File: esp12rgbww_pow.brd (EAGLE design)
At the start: 31.5 x 30 mm, 16 parts, among them J1 1X2-3.5MM, J2 1X2-3.5MM, J3 1X2-3.5MM

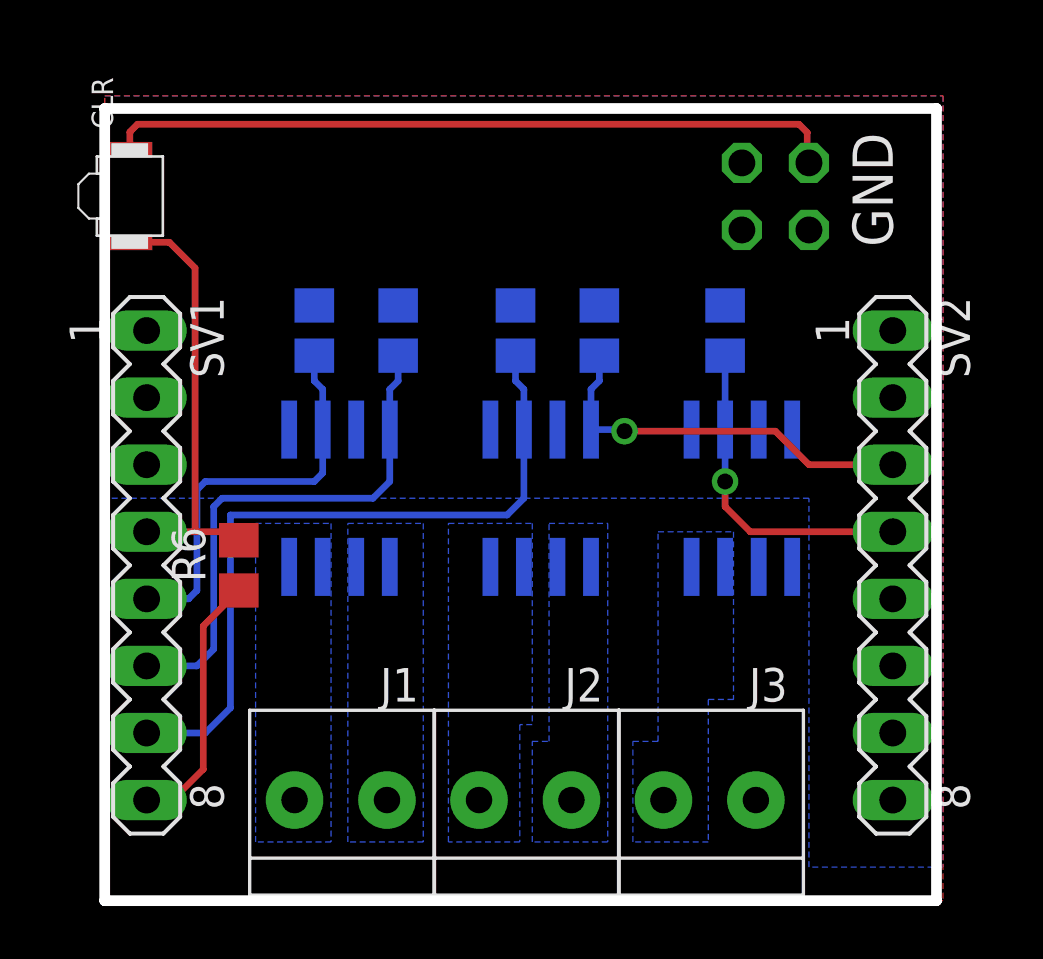
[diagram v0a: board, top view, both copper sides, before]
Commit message: FT232 module
FT232 Module now functional as a prototype
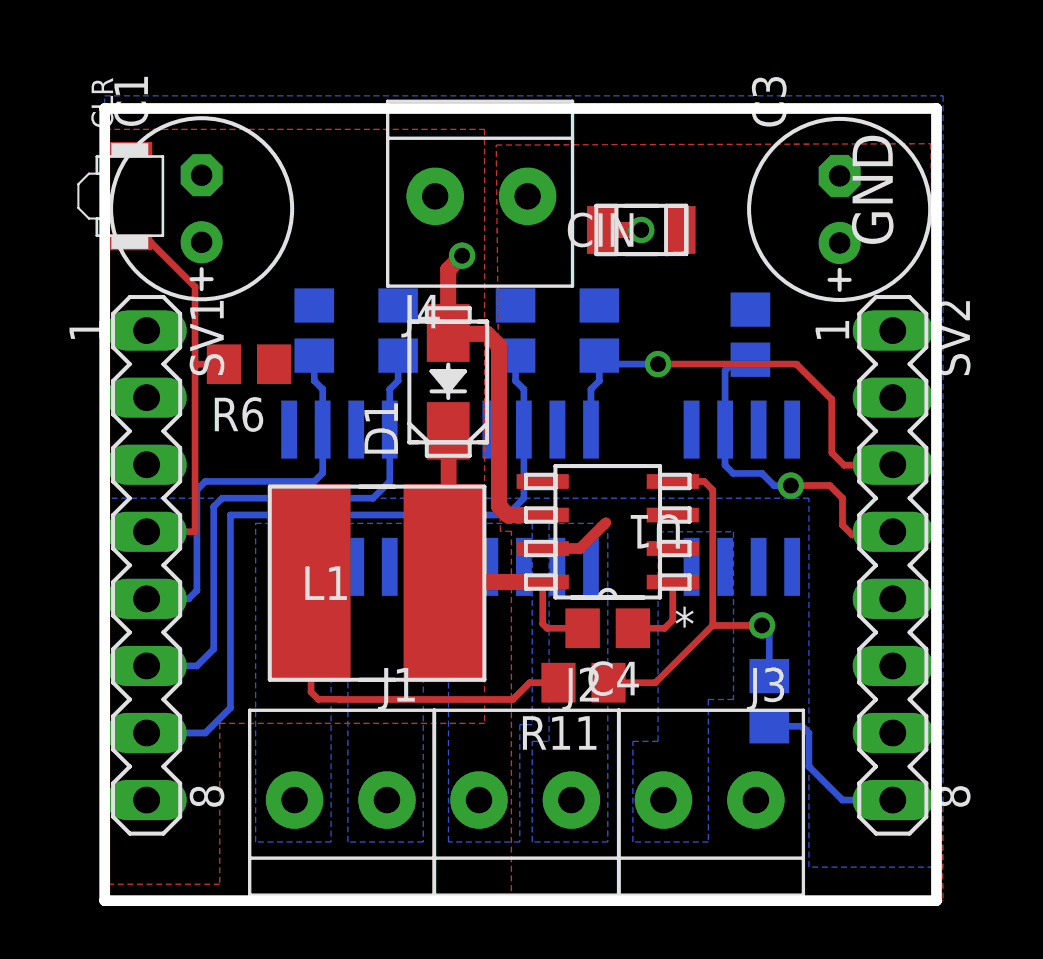
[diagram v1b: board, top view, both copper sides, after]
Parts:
- removed JP1: (no value), pinhead:2X02
- added C1: 440nF, resistor:E2,5-7
- added C3: 240uF, resistor:E2,5-7
- added C4: 10nF, resistor:C0805
- added CIN: 4.7uF, AcceleratedDesigns_Lib:1206
- added D1: 570mV, TI_Accelerated_Design_neu:SMA
- added J4: 1X2-3.5MM, adafruit:1X2-3.5MM
- added L1: 56uH, AcceleratedDesigns_Lib:IND_NPI75C
- added R11: 10k, resistor:R0805
- added R12: 5.9k, resistor:R0805
- added U1: TPS5410DR, AcceleratedDesigns_Lib:M08A
- moved R6 7.63 mm to (5.47, 20.3), turned to 180 degrees
- moved R1 0.97 mm to (24.5, 21.4)
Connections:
- new net BOOT: C4.1, U1.1
- new net PH: C4.2, D1.1, L1.2, U1.8
- new net SENS: R11.1, R12.2, U1.4
- net +12V: now also C3.+, CIN.2, J4.2, U1.7; no longer JP1.1, JP1.3
- net GND: now also C1.-, C3.-, CIN.1, D1.2, J4.1, R12.1, U1.6; no longer JP1.2, JP1.4
- net VCC: now also C1.+, L1.1, R11.2
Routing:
- net SENS: track 0.00 -> 15.5 mm, vias 0 -> 1
- net PH: track 0.00 -> 12.9 mm
- net GND: track 27.8 -> 21.3 mm, vias 0 -> 2
- net VCC: track 9.96 -> 14.3 mm
- net BOOT: track 0.00 -> 3.08 mm
- net +12V: track 0.00 -> 2.80 mm
- net GPIO5: track 14.9 -> 17.0 mm
- net GPIO16: track 16.5 -> 15.4 mm
- added copper zone on layer 1, net VCC
